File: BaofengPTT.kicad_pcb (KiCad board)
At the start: 2 copper layers, 61.6 x 58.4 mm, 8 parts, among them CON1 SJ1-3523N, CON2 SJ1-3523N, CON3 SJ1-3523N, CON4 SJ1-3523N, Q1 BSS138

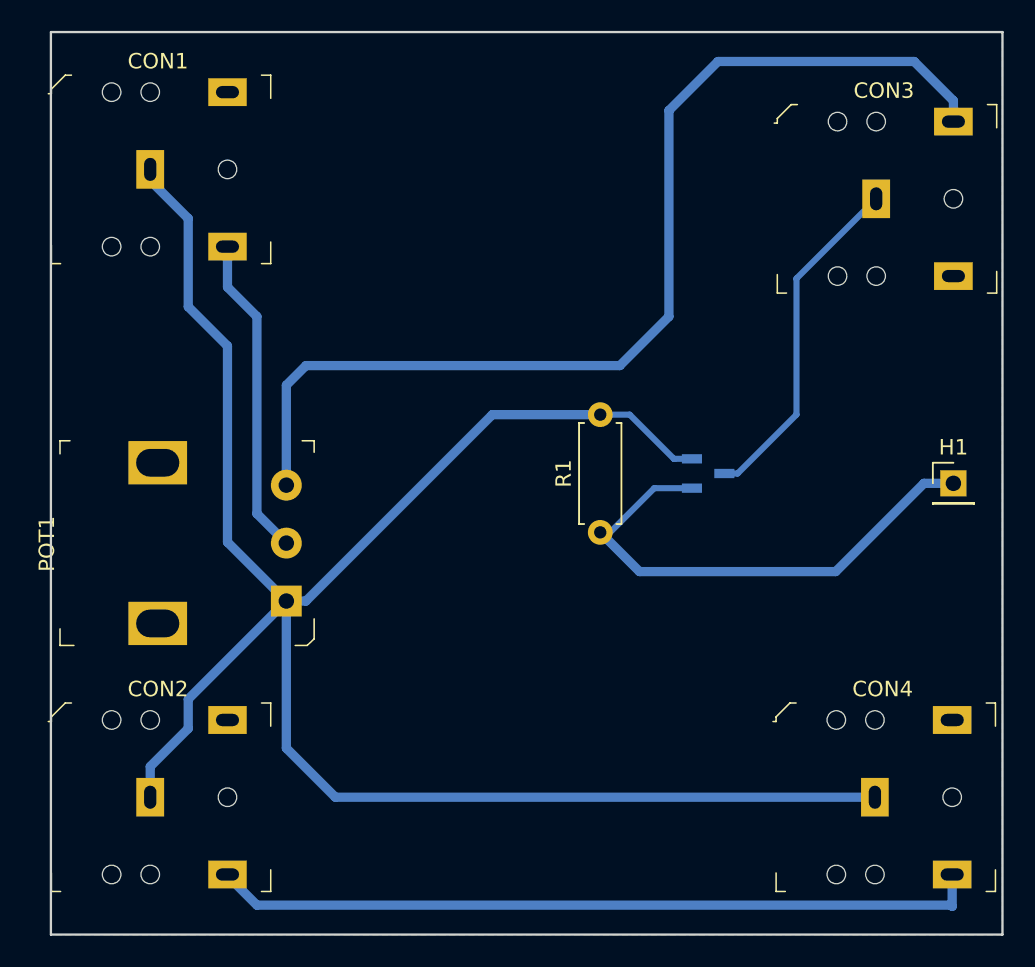
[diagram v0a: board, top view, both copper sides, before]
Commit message: added dc block capacitor
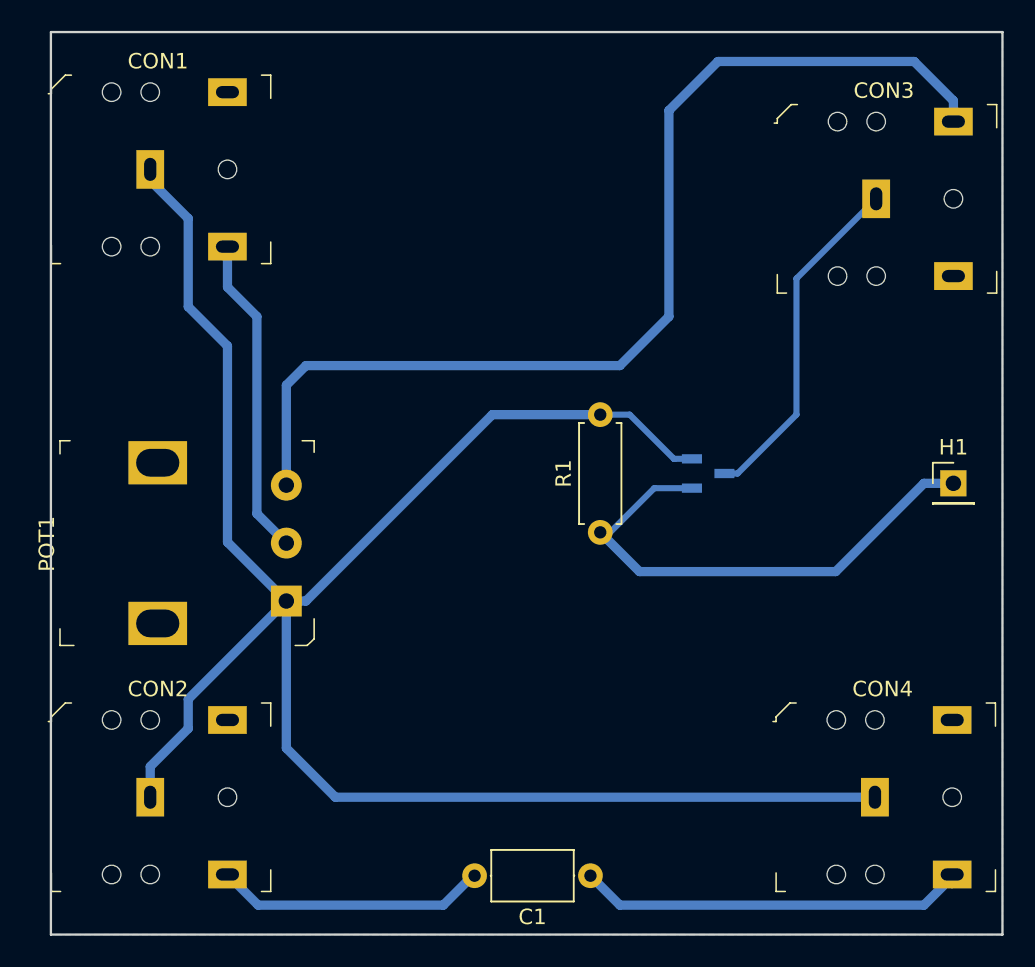
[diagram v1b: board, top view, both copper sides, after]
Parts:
- added C1: .1 uF, Capacitor_THT:C_Axial_L5.1mm_D3.1mm_P7.50mm_Horizontal, F.Cu at (121.3, 113.0)
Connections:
- CON2 pad 2: Net-(CON2-Pad2) -> Net-(C1-Pad2)
- CON4 pad 2: Net-(CON2-Pad2) -> Net-(C1-Pad1)
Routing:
- net Net-(CON2-Pad2): track 49.9 -> 0.00 mm
- net Net-(C1-Pad1): track 0.00 -> 25.9 mm
- net Net-(C1-Pad2): track 0.00 -> 17.7 mm

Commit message: added resitor to lower input level to sound card, placed top side coppor pour
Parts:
- added R2: 82, Resistor_THT:R_Axial_DIN0207_L6.3mm_D2.5mm_P7.62mm_Horizontal, F.Cu at (113.7, 113.0)
- moved C1 6.35 mm to (127.6, 113.0)
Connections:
- CON2 pad 2: Net-(C1-Pad2) -> Net-(CON2-Pad2)
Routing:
- net Net-(C1-Pad2): track 17.7 -> 6.47 mm
- net Net-(CON2-Pad2): track 0.00 -> 8.37 mm
- net Net-(C1-Pad1): track 25.9 -> 19.6 mm
- added copper zone on F.Cu, net Net-(CON1-Pad1)
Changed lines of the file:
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@@
     (tracks 55)
     (zones 0)
-    (modules 9)
-    (nets 13)
+    (modules 10)
+    (nets 14)
   )
   (page A4)
@@
   (net 11 "Net-(C1-Pad1)")
   (net 12 "Net-(C1-Pad2)")
+  (net 13 "Net-(CON2-Pad2)")
   (net_class Default "This is the default net class."
     (clearance 0.2)
@@
     (add_net "Net-(CON1-Pad2)")
     (add_net "Net-(CON1-Pad3)")
+    (add_net "Net-(CON2-Pad2)")
     (add_net "Net-(CON2-Pad3)")
     (add_net "Net-(CON3-Pad1)")
@@
       (net 3 "Net-(CON1-Pad1)"))
     (pad 2 thru_hole rect (at 0 5) (size 2.5 1.8) (drill oval 1.5 0.8) (layers *.Cu *.Mask)
-      (net 12 "Net-(C1-Pad2)"))
+      (net 13 "Net-(CON2-Pad2)"))
     (pad 3 thru_hole rect (at 0 -5) (size 2.5 1.8) (drill oval 1.5 0.8) (layers *.Cu *.Mask)
       (net 4 "Net-(CON2-Pad3)"))
@@
   )
   (module Capacitor_THT:C_Axial_L5.1mm_D3.1mm_P7.50mm_Horizontal (layer F.Cu)
-    (at 121.285 113.03 180)
+    (at 127.635 113.03 180)
     (descr "C, Axial series, Axial, Horizontal, pin pitch=7.5mm, , length*diameter=5.1*3.1mm^2, http://www.vishay.com/docs/45231/arseries.pdf")
     (tags "C Axial series Axial Horizontal pin pitch 7.5mm  length 5.1mm diameter 3.1mm")
@@
     (fp_line (start 8.55 1.8) (end 8.55 -1.8) (layer F.CrtYd) (width 0.05))
     (fp_line (start 8.55 -1.8) (end -1.05 -1.8) (layer F.CrtYd) (width 0.05))
-    (fp_text user %R (at 3.75 0 180) (layer F.Fab)
+    (fp_text user %R (at 3.81 0 180) (layer F.Fab)
       (effects (font (size 1 1) (thickness 0.15)))
     )
@@
       (net 12 "Net-(C1-Pad2)"))
     (model ${KISYS3DMOD}/Capacitor_THT.3dshapes/C_Axial_L5.1mm_D3.1mm_P7.50mm_Horizontal.wrl
+      (at (xyz 0 0 0))
+      (scale (xyz 1 1 1))
+      (rotate (xyz 0 0 0))
+    )
+  )
+  (module Resistor_THT:R_Axial_DIN0207_L6.3mm_D2.5mm_P7.62mm_Horizontal (layer F.Cu)
+    (at 113.665 113.03 180)
+    (descr "Resistor, Axial_DIN0207 series, Axial, Horizontal, pin pitch=7.62mm, 0.25W = 1/4W, length*diameter=6.3*2.5mm^2, http://cdn-reichelt.de/documents/datenblatt/B400/1_4W%23YAG.pdf")
+    (tags "Resistor Axial_DIN0207 series Axial Horizontal pin pitch 7.62mm 0.25W = 1/4W length 6.3mm diameter 2.5mm")
+    (fp_text reference R2 (at 3.81 -2.37 180) (layer F.SilkS)
+      (effects (font (size 1 1) (thickness 0.15)))
+    )
+    (fp_text value 82 (at 3.81 2.37 180) (layer F.Fab)
+      (effects (font (size 1 1) (thickness 0.15)))
+    )
+    (fp_line (start 0.66 -1.25) (end 0.66 1.25) (layer F.Fab) (width 0.1))
+    (fp_line (start 0.66 1.25) (end 6.96 1.25) (layer F.Fab) (width 0.1))
+    (fp_line (start 6.96 1.25) (end 6.96 -1.25) (layer F.Fab) (width 0.1))
+    (fp_line (start 6.96 -1.25) (end 0.66 -1.25) (layer F.Fab) (width 0.1))
+    (fp_line (start 0 0) (end 0.66 0) (layer F.Fab) (width 0.1))
+    (fp_line (start 7.62 0) (end 6.96 0) (layer F.Fab) (width 0.1))
+    (fp_line (start 0.54 -1.04) (end 0.54 -1.37) (layer F.SilkS) (width 0.12))
+    (fp_line (start 0.54 -1.37) (end 7.08 -1.37) (layer F.SilkS) (width 0.12))
+    (fp_line (start 7.08 -1.37) (end 7.08 -1.04) (layer F.SilkS) (width 0.12))
+    (fp_line (start 0.54 1.04) (end 0.54 1.37) (layer F.SilkS) (width 0.12))
+    (fp_line (start 0.54 1.37) (end 7.08 1.37) (layer F.SilkS) (width 0.12))
+    (fp_line (start 7.08 1.37) (end 7.08 1.04) (layer F.SilkS) (width 0.12))
+    (fp_line (start -1.05 -1.5) (end -1.05 1.5) (layer F.CrtYd) (width 0.05))
+    (fp_line (start -1.05 1.5) (end 8.67 1.5) (layer F.CrtYd) (width 0.05))
+    (fp_line (start 8.67 1.5) (end 8.67 -1.5) (layer F.CrtYd) (width 0.05))
+    (fp_line (start 8.67 -1.5) (end -1.05 -1.5) (layer F.CrtYd) (width 0.05))
+    (fp_text user %R (at 3.81 0 180) (layer F.Fab)
+      (effects (font (size 1 1) (thickness 0.15)))
+    )
+    (pad 1 thru_hole circle (at 0 0 180) (size 1.6 1.6) (drill 0.8) (layers *.Cu *.Mask)
+      (net 12 "Net-(C1-Pad2)"))
+    (pad 2 thru_hole oval (at 7.62 0 180) (size 1.6 1.6) (drill 0.8) (layers *.Cu *.Mask)
+      (net 13 "Net-(CON2-Pad2)"))
+    (model ${KISYS3DMOD}/Resistor_THT.3dshapes/R_Axial_DIN0207_L6.3mm_D2.5mm_P7.62mm_Horizontal.wrl
       (at (xyz 0 0 0))
       (scale (xyz 1 1 1))
@@
   (segment (start 104.775 107.95) (end 101.6 104.775) (width 0.6) (layer B.Cu) (net 3))
   (segment (start 104.775 107.95) (end 139.7 107.95) (width 0.6) (layer B.Cu) (net 3))
-  (segment (start 97.79 112.95) (end 97.79 113.03) (width 0.6) (layer B.Cu) (net 12))
   (segment (start 144.78 64.215) (end 144.78 64.135) (width 0.6) (layer B.Cu) (net 5))
   (segment (start 144.78 64.215) (end 144.78 62.865) (width 0.6) (layer B.Cu) (net 5))
@@
   (segment (start 144.7 112.95) (end 144.7 113.745) (width 0.25) (layer B.Cu) (net 11))
   (segment (start 144.7 112.95) (end 144.7 113.11) (width 0.6) (layer B.Cu) (net 11))
-  (segment (start 144.7 113.11) (end 142.875 114.935) (width 0.6) (layer B.Cu) (net 11))
-  (segment (start 123.19 114.935) (end 121.285 113.03) (width 0.6) (layer B.Cu) (net 11))
-  (segment (start 142.875 114.935) (end 123.19 114.935) (width 0.6) (layer B.Cu) (net 11))
-  (segment (start 113.785 113.03) (end 113.665 113.03) (width 0.6) (layer B.Cu) (net 12))
-  (segment (start 113.665 113.03) (end 111.76 114.935) (width 0.6) (layer B.Cu) (net 12))
-  (segment (start 99.775 114.935) (end 97.79 112.95) (width 0.6) (layer B.Cu) (net 12))
-  (segment (start 111.76 114.935) (end 99.775 114.935) (width 0.6) (layer B.Cu) (net 12))
+  (segment (start 127.635 113.03) (end 130.175 113.03) (width 0.6) (layer B.Cu) (net 11))
+  (segment (start 130.175 113.03) (end 132.08 114.935) (width 0.6) (layer B.Cu) (net 11))
+  (segment (start 142.715 114.935) (end 144.7 112.95) (width 0.6) (layer B.Cu) (net 11))
+  (segment (start 132.08 114.935) (end 142.715 114.935) (width 0.6) (layer B.Cu) (net 11))
+  (segment (start 113.665 113.03) (end 120.135 113.03) (width 0.6) (layer B.Cu) (net 12))
+  (segment (start 97.79 112.95) (end 97.79 113.03) (width 0.6) (layer B.Cu) (net 13))
+  (segment (start 105.965 112.95) (end 106.045 113.03) (width 0.6) (layer B.Cu) (net 13))
+  (segment (start 97.79 112.95) (end 105.965 112.95) (width 0.6) (layer B.Cu) (net 13))
+  (zone (net 3) (net_name "Net-(CON1-Pad1)") (layer B.Cu) (hatch edge 0.508)
+    (connect_pads (clearance 0.508))
+    (min_thickness 0.254)
+    (fill (arc_segments 16) (thermal_gap 0.508) (thermal_bridge_width 0.508))
+    (polygon
+      (pts
+        (xy 86.36 58.42) (xy 147.955 58.42) (xy 147.955 116.84) (xy 86.36 116.84) (xy 86.36 115.57)
+      )
+    )
+  )
   (zone (net 3) (net_name "Net-(CON1-Pad1)") (layer B.Cu) (hatch edge 0.508)
     (connect_pads (clearance 0.508))
@@
     (polygon
       (pts
-        (xy 86.36 58.42) (xy 147.955 58.42) (xy 147.955 116.84) (xy 86.36 116.84) (xy 86.36 115.57)
+        (xy 86.36 58.42) (xy 147.955 58.42) (xy 147.955 116.84) (xy 86.36 116.84) (xy 86.36 111.76)
       )
     )
+  )
+  (zone (net 3) (net_name "Net-(CON1-Pad1)") (layer F.Cu) (hatch edge 0.508)
+    (connect_pads (clearance 0.508))
+    (min_thickness 0.254)
+    (fill yes (arc_segments 16) (thermal_gap 0.508) (thermal_bridge_width 0.508))
+    (polygon
+      (pts
+        (xy 86.36 58.42) (xy 147.955 58.42) (xy 147.955 116.84) (xy 86.36 116.84)
+      )
+    )
